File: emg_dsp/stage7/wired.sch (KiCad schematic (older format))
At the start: 54 parts, among them U38 OMNETICS_36, U41 MIC5365-2.5, U42 TC1016-3.0, U43 TC1016-3.0, U44 AD7980, U45 AD7980, U46 ADR381, U47 8X100, U48 8X100, U49 TC1016-3.0, U50 IL715-3, U51 DCP01DB, U52 IL715-3, U92 RHA2116, U93 RHA2116

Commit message: adding changes to new board -- still feel that the schematic needs to be checked over, though.
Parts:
- removed C100, C101, C102: 10uf, 0603, symbol C
- removed C222, C223, C224, C89, C90, C91, C92, C94, C95: 0.1uf, 0402, symbol C
- removed C85, C86, C88, C96, C97, C98, C99: 2.2uf, 0402, symbol C
- removed L11: ferrite, 0402, symbol INDUCTOR
- removed R82, R85: 15k, 0402, symbol R
- removed R83, R86: 25.2k, 0402, symbol R
- removed R84, R87: 7.5k, 0402, symbol R
- removed R88, R89, R91, R92, R93: 200, 0402, symbol R
- removed U38: OMNETICS_36, omnetics_36, symbol OMNETICS_36
- removed U41: MIC5365-2.5, SC-70-5, symbol MIC5365
- removed U42, U43: TC1016-3.0, SC-70-5, symbol TC1016
- removed U44, U45: AD7980, MSOP-10, symbol AD7980
- removed U46: ADR381, SOT-23, symbol ADR381
- removed U47: 8X100, 8xWx100mil, symbol 8X100
- removed U48: 8X100, 8x100mil, symbol 8X100
- removed U50: IL715-3, SOIC-16, symbol ADUM2400
- removed U92, U93: RHA2116, QFN-40, symbol RHA2116
- added R70, R71, R72: 200, 0402, symbol R
- added U42: 9X100, omnetics_9, symbol 9X100
- C87: value 2.2uf -> 200uf; footprint 0402 -> 2917
- C93: value 2.2uf -> 10uf; footprint 0402 -> 0603
- renumbered C104 to C88, C103 to C89, C105 to C90, C221 to C91, C256 to C92, R90 to R73, U49 to U43, U51 to U44, U52 to U45
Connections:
- net labels added: DT0PRI, DT0SEC, TFS0, TSCLK0
- net labels removed: D0, D1, E1, E10, E11, E12, E13, E14, E15, E16, E17, E18, E19, E2, E20, E21, E22, E23, E24, E25, E26, E27, E28, E29, E3, E30, E31, E32, E4, E5, E6, E7, E8, E9, RCLK, RESET, RFS, STEP, V0, V25, V3, V3B, V5, VREF, _reset, isorclk, isorfs, isostep, sd0, sd1
- wire segments 258 -> 43
- no-connect marks 14 -> 2
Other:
- note removed: "MIC5365-2.5YC5"
- note removed: "it seems we do not need"
- note removed: "this ADC has 14 ENOB"
- note removed: "to gate this clock."
- note removed: "when vref = 2.5v,"
- moved on the sheet: C88, C91, C92, R73, U44

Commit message: schematic improvements / modifications.
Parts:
- added C?: 0.1uf, 0402, symbol C
- added C?: 2.2uf, 0402, symbol C
- added R?: 22k, 0402, symbol R
- added R?: 94k, 0402, symbol R
- added U?: LT1721, SSOP-16, symbol LT1721
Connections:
- net V0b: now also C?.1, C?.2, R?.1, U?.3 (GND), U?.6 (GND)
- net V3C: now also C?.2, U?.11 (VCC), U?.14 (VCC)
- net at R73.2, U42.2: now also U?.15 (+IND); no longer U45.6 (Vin_D)
- net at R70.2, U42.8: now also U?.2 (+INA); no longer U45.3 (Vin_A)
- net at R71.2, U42.6: now also U?.7 (+INB); no longer U45.4 (Vin_B)
- net at R72.2, U42.4: now also U?.10 (+INC); no longer U45.5 (Vin_C)
- new net: U45.3 (Vin_A), U?.4 (OUTA)
- new net: U45.4 (Vin_B), U?.5 (OUTB)
- new net: U45.5 (Vin_C), U?.12 (OUTC)
- new net: U45.6 (Vin_D), U?.13 (OUTD)
- new net: C?.1, R?.1, R?.2, U?.1 (-INA), U?.16 (-IND), U?.8 (-INB), U?.9 (-INC)
- new net V3b: R?.2
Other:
- note added: "headstage operating at 2.7v -> 1.35V output. Threshold @ 0.7v"
- note removed: "this regulator is on the bridge"
- moved on the sheet: R70, R71, R72, R73, U42

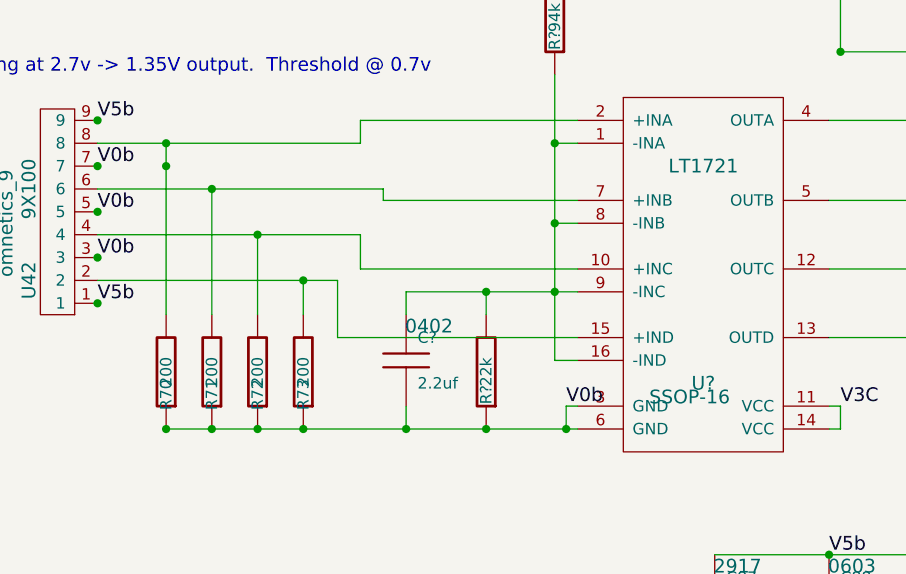
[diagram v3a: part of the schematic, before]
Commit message: working on the stimulator - using battery isolation for now. the Burr-brown DC-DC converters tend to generate a bit of noise.
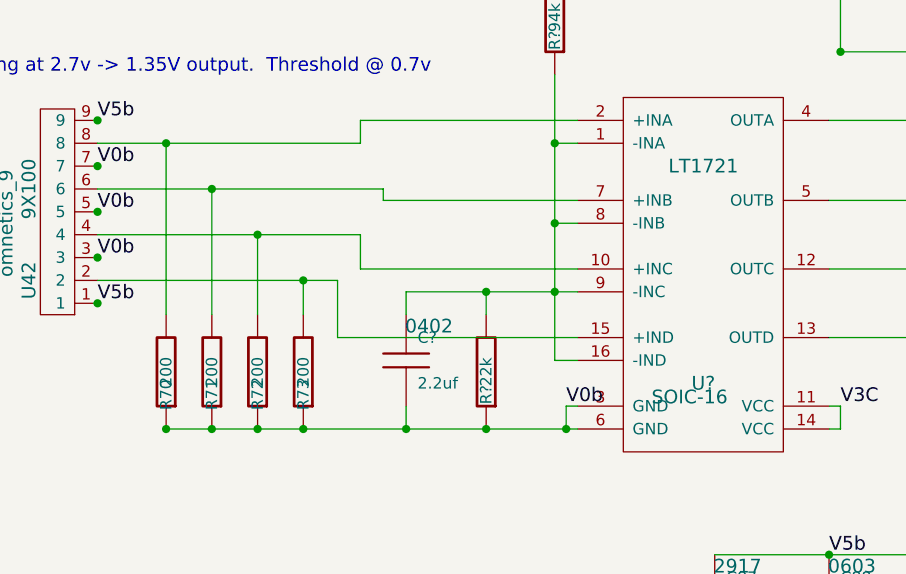
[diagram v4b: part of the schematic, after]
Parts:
- U?: footprint SSOP-16 -> SOIC-16
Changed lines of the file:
@@
-EESchema Schematic File Version 2  date Fri 21 Jan 2011 02:51:55 PM EST
+EESchema Schematic File Version 2  date Fri 21 Jan 2011 05:22:11 PM EST
 LIBS:power
 LIBS:device
@@
 Sheet 2 19
 Title "Stage 4 / Copyright 2010 Timothy L Hanson "
-Date "20 jan 2011"
+Date "21 jan 2011"
 Rev ""
 Comp "This design is free: redistribute or modify under the GPL v. 3 or later"
@@
 Wire Wire Line
 	11600 3150 11600 2800
-Connection ~ 6650 3650
 Wire Wire Line
 	6650 3550 6650 4300
@@
 F 0 "U?" H 9000 3600 60  0000 C CNN
 F 1 "LT1721" H 9000 4550 60  0000 C CNN
-F 2 "SSOP-16" H 8940 3540 60  0000 C CNN
+F 2 "SOIC-16" H 8940 3540 60  0000 C CNN
 	1    9000 4100
 	1    0    0    -1

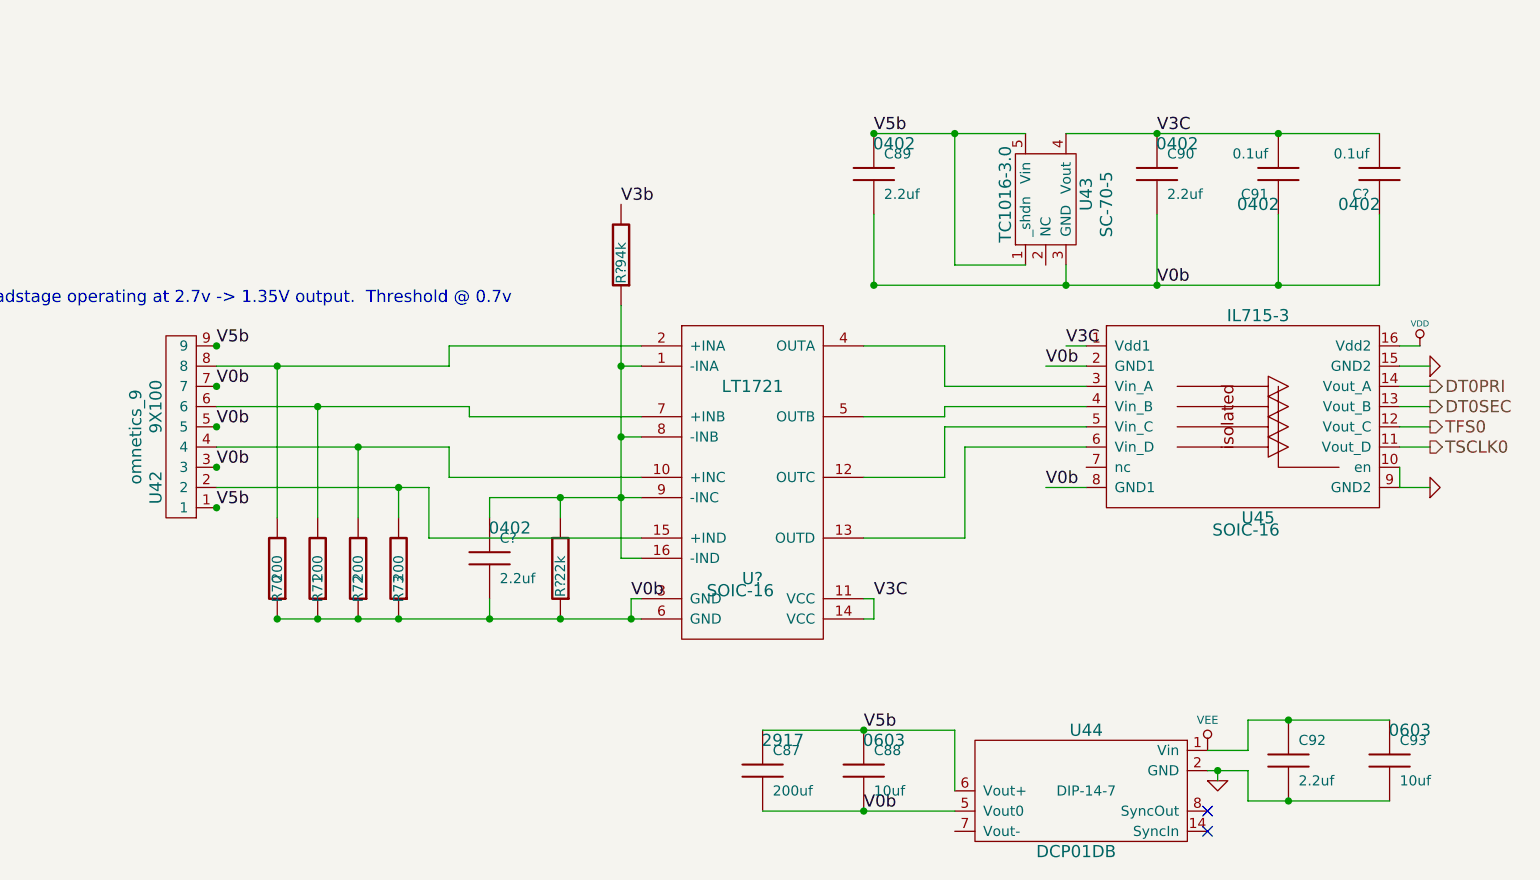
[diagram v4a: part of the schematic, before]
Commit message: starting placement of modules in board...
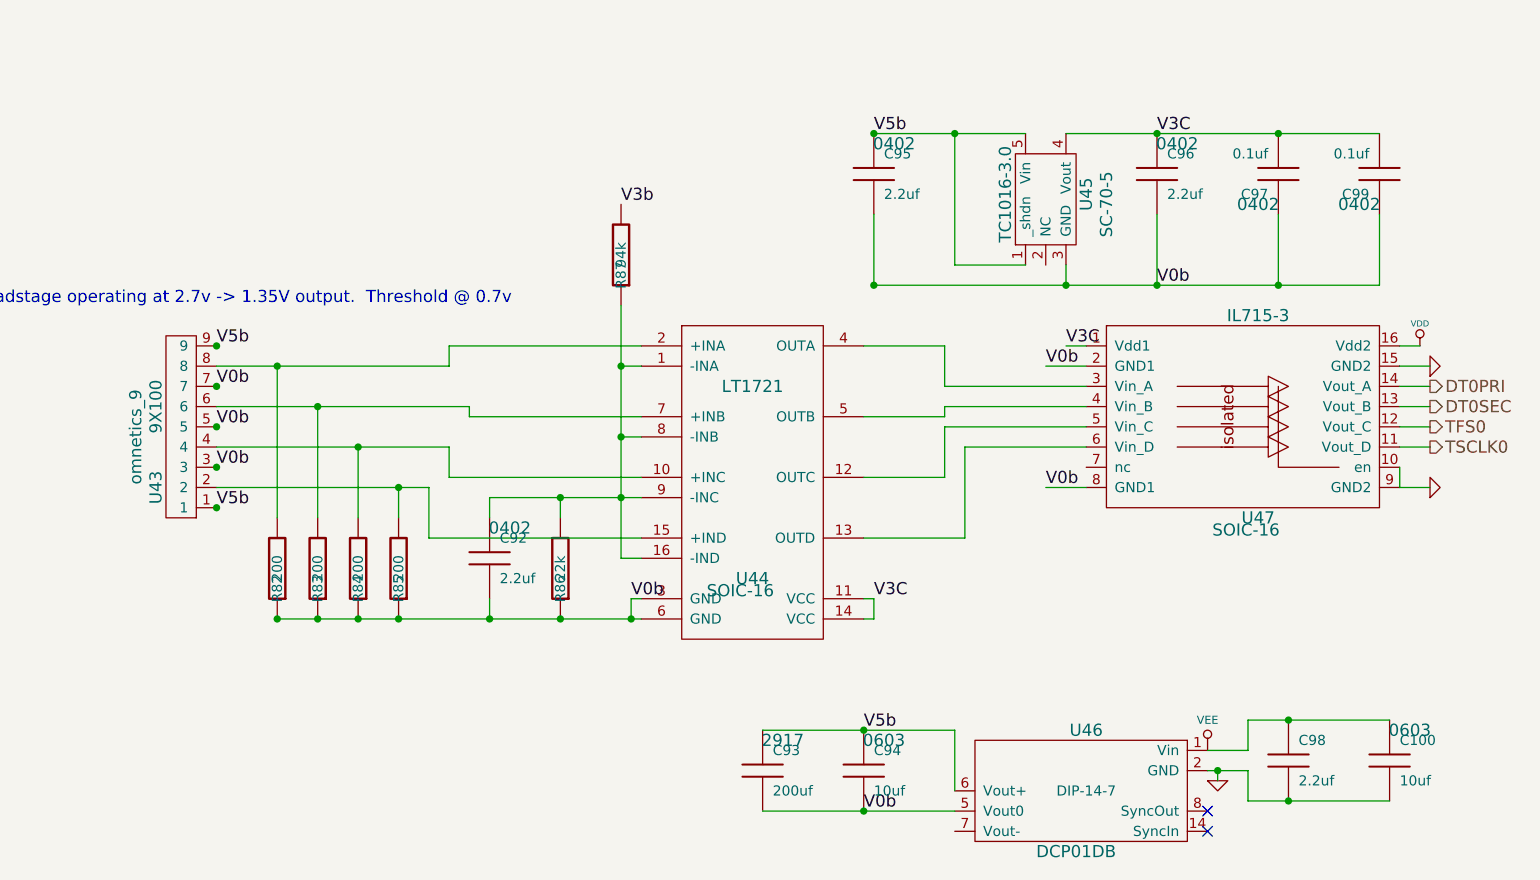
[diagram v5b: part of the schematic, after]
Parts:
- gave numbers to parts that had none: 5
- renumbered C93 to C100, C87 to C93, C88 to C94, C89 to C95, C90 to C96, C91 to C97, C92 to C98, R70 to R82, R71 to R83, R72 to R84, R73 to R85, U42 to U43, U43 to U45, U44 to U46, U45 to U47
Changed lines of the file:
@@
-EESchema Schematic File Version 2  date Fri 21 Jan 2011 05:22:11 PM EST
+EESchema Schematic File Version 2  date Fri 21 Jan 2011 07:08:04 PM EST
 LIBS:power
 LIBS:device
@@
 Sheet 2 19
 Title "Stage 4 / Copyright 2010 Timothy L Hanson "
-Date "21 jan 2011"
+Date "22 jan 2011"
 Rev ""
 Comp "This design is free: redistribute or modify under the GPL v. 3 or later"
@@
 Connection ~ 8050 4200
 $Comp
-L C C?
+L C C92
 U 1 1 4D3897A9
 P 7700 4500
-F 0 "C?" H 7750 4600 50  0000 L CNN
+F 0 "C92" H 7750 4600 50  0000 L CNN
 F 1 "2.2uf" H 7750 4400 50  0000 L CNN
 F 2 "0402" H 7800 4650 60  0000 C CNN
@@
 V3b
 $Comp
-L R R?
+L R R87
 U 1 1 4D38973E
 P 8350 3000
-F 0 "R?" V 8350 3100 50  0000 C CNN
+F 0 "R87" V 8350 3100 50  0000 C CNN
 F 1 "94k" V 8350 3000 50  0000 C CNN
 F 2 "0402" V 8480 2950 60  0001 C CNN
@@
 $EndComp
 $Comp
-L R R?
+L R R86
 U 1 1 4D3896D7
 P 8050 4550
-F 0 "R?" V 8050 4650 50  0000 C CNN
+F 0 "R86" V 8050 4650 50  0000 C CNN
 F 1 "22k" V 8050 4550 50  0000 C CNN
 F 2 "0402" V 8180 4500 60  0001 C CNN
@@
 V3C
 $Comp
-L C C?
+L C C99
 U 1 1 4D3895B6
 P 12100 2600
-F 0 "C?" H 12150 2700 50  0000 L CNN
+F 0 "C99" H 12150 2700 50  0000 L CNN
 F 1 "0.1uf" H 12150 2500 50  0000 L CNN
 F 2 "0402" H 12200 2750 60  0000 C CNN
@@
 $EndComp
 $Comp
-L LT1721 U?
+L LT1721 U44
 U 1 1 4D3895A0
 P 9000 4100
-F 0 "U?" H 9000 3600 60  0000 C CNN
+F 0 "U44" H 9000 3600 60  0000 C CNN
 F 1 "LT1721" H 9000 4550 60  0000 C CNN
 F 2 "SOIC-16" H 8940 3540 60  0000 C CNN
@@
 $EndComp
 $Comp
-L C C93
+L C C100
 U 1 1 4D360B24
 P 12150 5500
-F 0 "C93" H 12200 5600 50  0000 L CNN
+F 0 "C100" H 12200 5600 50  0000 L CNN
 F 1 "10uf" H 12200 5400 50  0000 L CNN
 F 2 "0603" H 12250 5650 60  0000 C CNN
@@
 $EndComp
 $Comp
-L C C87
+L C C93
 U 1 1 4D360AD0
 P 9050 5550
-F 0 "C87" H 9100 5650 50  0000 L CNN
+F 0 "C93" H 9100 5650 50  0000 L CNN
 F 1 "200uf" H 9100 5450 50  0000 L CNN
 F 2 "2917" H 9150 5700 60  0000 C CNN
@@
 $EndComp
 $Comp
-L R R70
+L R R82
 U 1 1 4D360A45
 P 6650 4550
-F 0 "R70" V 6650 4650 50  0000 C CNN
+F 0 "R82" V 6650 4650 50  0000 C CNN
 F 1 "200" V 6650 4550 50  0000 C CNN
 F 2 "0402" V 6780 4500 60  0001 C CNN
@@
 $EndComp
 $Comp
-L R R71
+L R R83
 U 1 1 4D360A27
 P 6850 4550
-F 0 "R71" V 6850 4650 50  0000 C CNN
+F 0 "R83" V 6850 4650 50  0000 C CNN
 F 1 "200" V 6850 4550 50  0000 C CNN
 F 2 "0402" V 6980 4500 60  0001 C CNN
@@
 $EndComp
 $Comp
-L R R72
+L R R84
 U 1 1 4D360A22
 P 7050 4550
-F 0 "R72" V 7050 4650 50  0000 C CNN
+F 0 "R84" V 7050 4650 50  0000 C CNN
 F 1 "200" V 7050 4550 50  0000 C CNN
 F 2 "0402" V 7180 4500 60  0001 C CNN
@@
 V5b
 $Comp
-L 9X100 U42
+L 9X100 U43
 U 1 1 4D360904
 P 6150 3800
-F 0 "U42" H 5800 3700 60  0000 C CNN
+F 0 "U43" H 5800 3700 60  0000 C CNN
 F 1 "9X100" H 6200 3700 60  0000 C CNN
 F 2 "omnetics_9" H 6050 3600 60  0000 C CNN
@@
 $EndComp
 $Comp
-L ADUM2400 U45
+L ADUM2400 U47
 U 1 1 4C9B7F27
 P 11500 4000
-F 0 "U45" H 11500 3700 60  0000 C CNN
+F 0 "U47" H 11500 3700 60  0000 C CNN
 F 1 "IL715-3" H 11500 4700 60  0000 C CNN
 F 2 "SOIC-16" H 11440 3640 60  0000 C CNN
@@
 TFS0
 $Comp
-L C C92
+L C C98
 U 1 1 4CAAB0E7
 P 11650 5500
-F 0 "C92" H 11700 5600 50  0000 L CNN
+F 0 "C98" H 11700 5600 50  0000 L CNN
 F 1 "2.2uf" H 11700 5400 50  0000 L CNN
 F 2 "0402" H 11750 5650 60  0001 C CNN
@@
 $EndComp
 $Comp
-L C C91
+L C C97
 U 1 1 4CA0EC72
 P 11600 2600
-F 0 "C91" H 11650 2700 50  0000 L CNN
+F 0 "C97" H 11650 2700 50  0000 L CNN
 F 1 "0.1uf" H 11650 2500 50  0000 L CNN
 F 2 "0402" H 11700 2750 60  0000 C CNN
@@
 NoConn ~ 11250 5750
 $Comp
-L GND #PWR0138
+L GND #PWR0139
 U 1 1 4C9B9212
 P 12350 4150
-F 0 "#PWR0138" H 12350 4150 30  0001 C CNN
+F 0 "#PWR0139" H 12350 4150 30  0001 C CNN
 F 1 "GND" H 12350 4080 30  0001 C CNN
 	1    12350 4150
@@
 $EndComp
 $Comp
-L GND #PWR0139
+L GND #PWR0140
 U 1 1 4C9B920A
 P 12350 3550
-F 0 "#PWR0139" H 12350 3550 30  0001 C CNN
+F 0 "#PWR0140" H 12350 3550 30  0001 C CNN
 F 1 "GND" H 12350 3480 30  0001 C CNN
 	1    12350 3550
@@
 $EndComp
 $Comp
-L VDD #PWR0140
+L VDD #PWR0141
 U 1 1 4C9B9204
 P 12300 3450
-F 0 "#PWR0140" H 12300 3550 30  0001 C CNN
+F 0 "#PWR0141" H 12300 3550 30  0001 C CNN
 F 1 "VDD" H 12300 3560 30  0000 C CNN
 	1    12300 3450
@@
 V5b
 $Comp
-L C C90
+L C C96
 U 1 1 4C9B9135
 P 11000 2600
-F 0 "C90" H 11050 2700 50  0000 L CNN
+F 0 "C96" H 11050 2700 50  0000 L CNN
 F 1 "2.2uf" H 11050 2500 50  0000 L CNN
 F 2 "0402" H 11100 2750 60  0000 C CNN
@@
 $EndComp
 $Comp
-L C C89
+L C C95
 U 1 1 4C9B9134
 P 9600 2600
-F 0 "C89" H 9650 2700 50  0000 L CNN
+F 0 "C95" H 9650 2700 50  0000 L CNN
 F 1 "2.2uf" H 9650 2500 50  0000 L CNN
 F 2 "0402" H 9700 2750 60  0000 C CNN
@@
 $EndComp
 $Comp
-L TC1016 U43
+L TC1016 U45
 U 1 1 4C9B9133
 P 10450 2700
-F 0 "U43" H 10450 2500 60  0000 C CNN
+F 0 "U45" H 10450 2500 60  0000 C CNN
 F 1 "TC1016-3.0" H 10450 2900 60  0000 C CNN
 F 2 "SC-70-5" H 10400 2400 60  0000 C CNN
@@
 V0b
 $Comp
-L C C88
+L C C94
 U 1 1 4C9B87D9
 P 9550 5550
-F 0 "C88" H 9600 5650 50  0000 L CNN
+F 0 "C94" H 9600 5650 50  0000 L CNN
 F 1 "10uf" H 9600 5450 50  0000 L CNN
 F 2 "0603" H 9650 5700 60  0000 C CNN
@@
 $EndComp
 $Comp
-L GND #PWR0141
+L GND #PWR0142
 U 1 1 4C9B8790
 P 11300 5600
-F 0 "#PWR0141" H 11300 5600 30  0001 C CNN
+F 0 "#PWR0142" H 11300 5600 30  0001 C CNN
 F 1 "GND" H 11300 5530 30  0001 C CNN
 	1    11300 5600
@@
 $EndComp
 $Comp
-L VEE #PWR196
+L VEE #PWR203
 U 1 1 4C9B878C
 P 11250 5450
-F 0 "#PWR196" H 11250 5650 40  0001 C CNN
+F 0 "#PWR203" H 11250 5650 40  0001 C CNN
 F 1 "VEE" H 11250 5600 40  0000 C CNN
 	1    11250 5450
@@
 $EndComp
 $Comp
-L DCP01DB U44
+L DCP01DB U46
 U 1 1 4C9B876F
 P 10650 5650
-F 0 "U44" H 10650 5950 60  0000 C CNN
+F 0 "U46" H 10650 5950 60  0000 C CNN
 F 1 "DCP01DB" H 10700 5350 60  0000 C CNN
 F 2 "DIP-14-7" H 10650 5650 50  0000 C CNN
@@
 $EndComp
 $Comp
-L R R73
+L R R85
 U 1 1 4C9ACC87
 P 7250 4550
-F 0 "R73" V 7250 4650 50  0000 C CNN
+F 0 "R85" V 7250 4650 50  0000 C CNN
 F 1 "200" V 7250 4550 50  0000 C CNN
 F 2 "0402" V 7380 4500 60  0001 C CNN
